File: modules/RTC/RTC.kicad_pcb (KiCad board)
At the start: 2 copper layers, 40.6 x 40.6 mm, 29 parts, among them J1 2, J10 11, J11 12, J12 13, J13 A0, J14 A1, J15 A2, J16 A3, J17 A4, J18 A5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

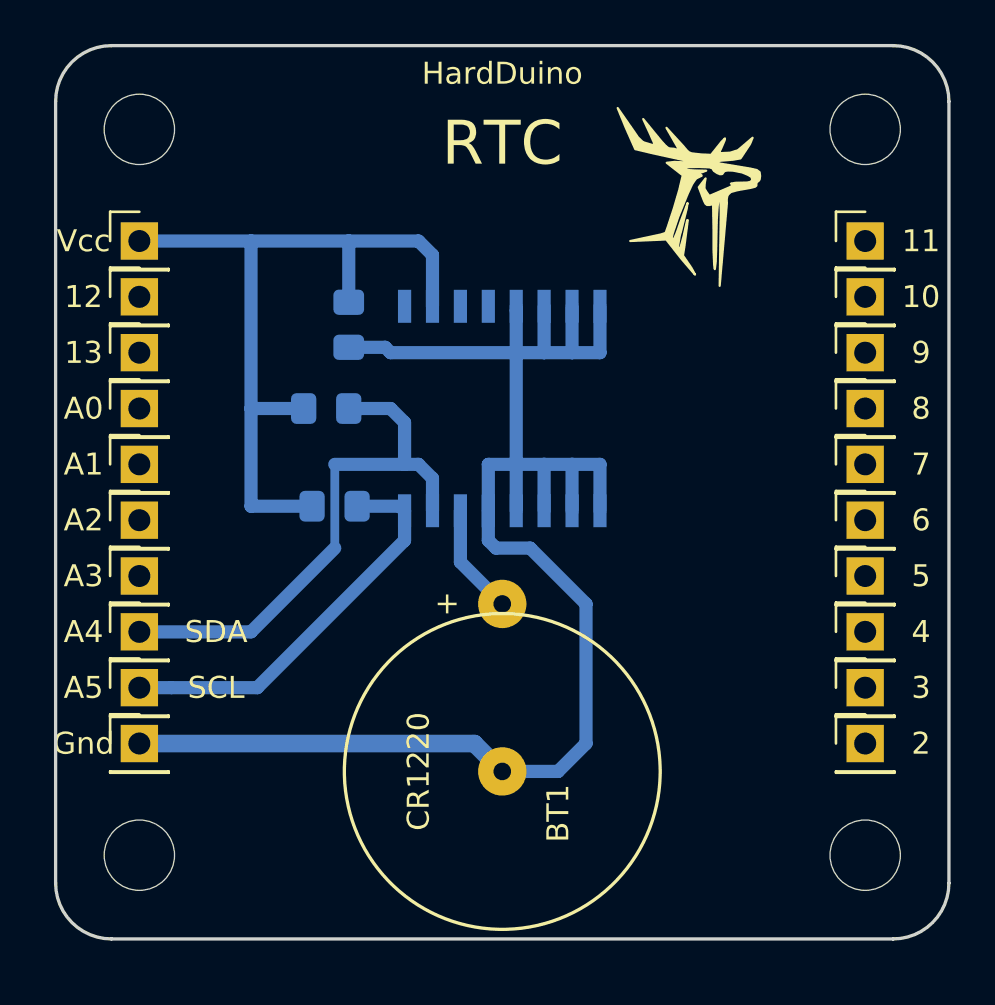
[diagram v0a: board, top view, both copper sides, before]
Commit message: 1x PCBs. Move holes to edges. Caution! This changes is uncompatible with previous versions...
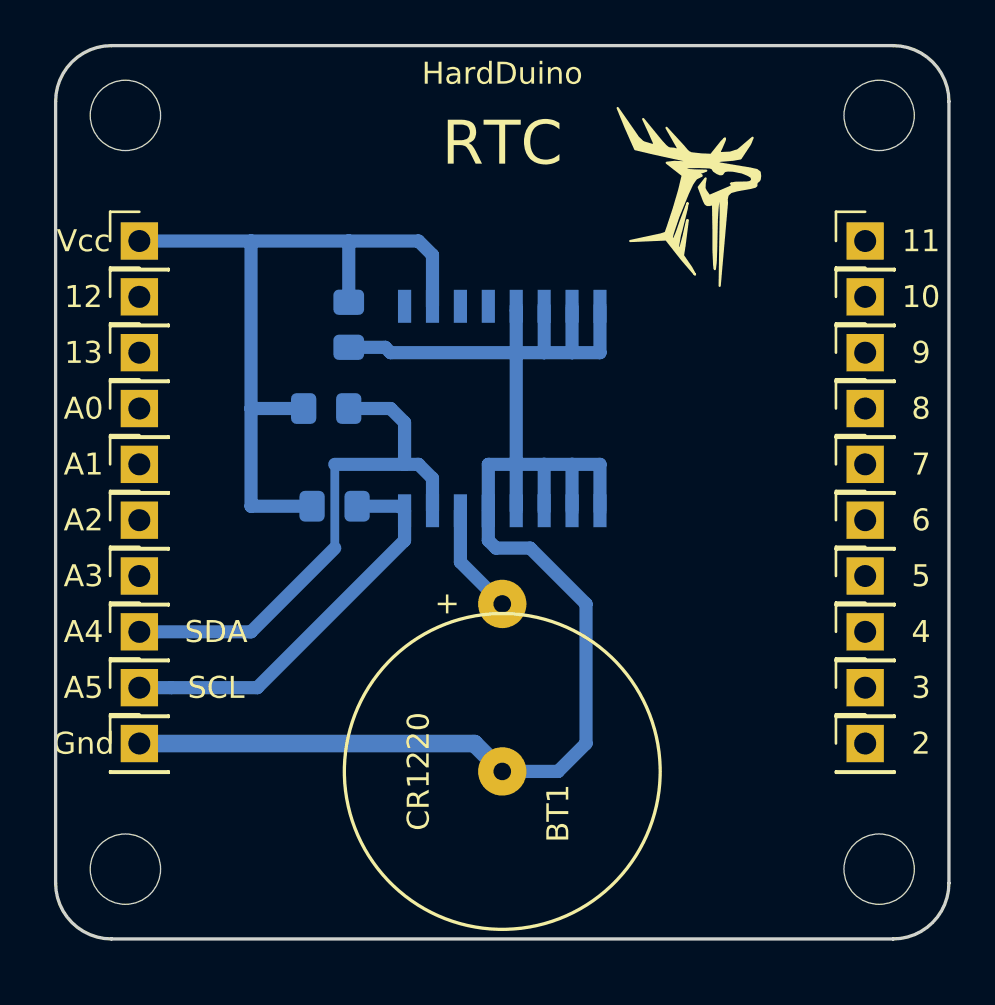
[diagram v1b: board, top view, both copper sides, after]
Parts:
- moved H2 0.90 mm to (92.1, 88.3)
- moved H4 0.90 mm to (126.4, 88.3)
- moved H1 0.90 mm to (92.1, 54.0)
- moved H3 0.90 mm to (126.4, 54.0)
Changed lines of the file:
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@@
   )
   (module MountingHole:MountingHole_3.2mm_M3 (layer F.Cu)
-    (at 92.71 54.61)
+    (at 92.0750 53.9750)
     (descr "Mounting Hole 3.2mm, no annular, M3")
     (tags "mounting hole 3.2mm no annular m3")
@@
   )
   (module MountingHole:MountingHole_3.2mm_M3 (layer F.Cu)
-    (at 92.71 87.63)
+    (at 92.0750 88.2650)
     (descr "Mounting Hole 3.2mm, no annular, M3")
     (tags "mounting hole 3.2mm no annular m3")
@@
   )
   (module MountingHole:MountingHole_3.2mm_M3 (layer F.Cu)
-    (at 125.73 54.61)
+    (at 126.3650 53.9750)
     (descr "Mounting Hole 3.2mm, no annular, M3")
     (tags "mounting hole 3.2mm no annular m3")
@@
   )
   (module MountingHole:MountingHole_3.2mm_M3 (layer F.Cu)
-    (at 125.73 87.63)
+    (at 126.3650 88.2650)
     (descr "Mounting Hole 3.2mm, no annular, M3")
     (tags "mounting hole 3.2mm no annular m3")

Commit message: Fix hash & version
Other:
- board text added: "21.02.2021"
- board text added: "b4d799"
- board text added: "v2.3"

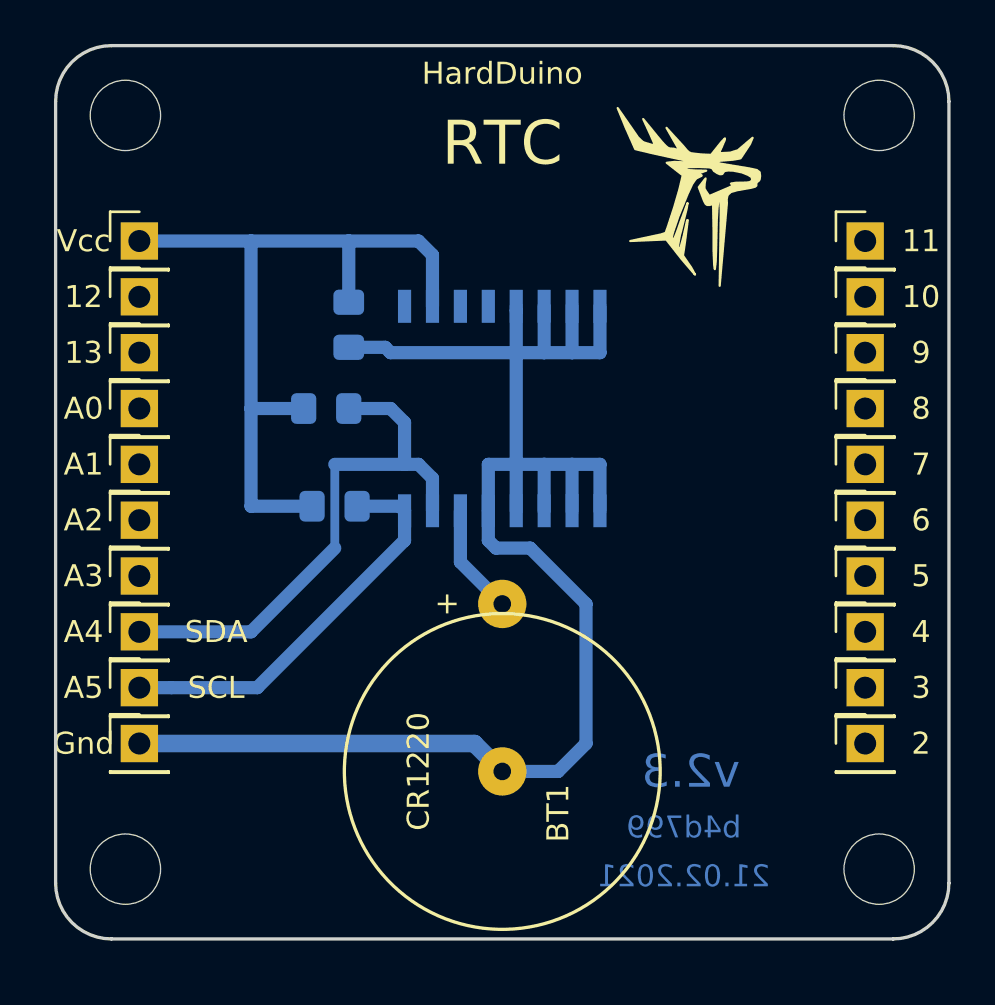
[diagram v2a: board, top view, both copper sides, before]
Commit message: All 1x shields was rotated clockwise
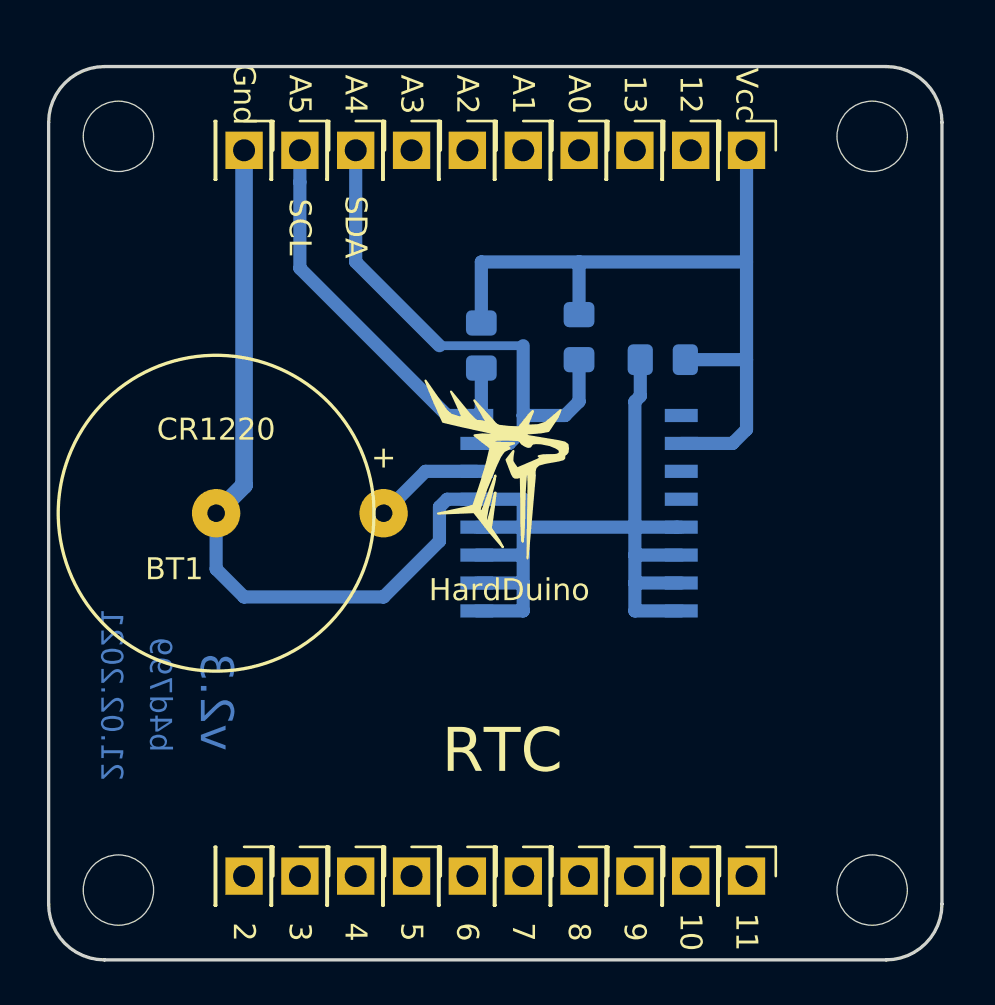
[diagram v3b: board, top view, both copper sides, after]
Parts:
- moved H3 35.2 mm to (126.0, 89.2), turned to 270 degrees
- moved H4 34.6 mm to (91.8, 89.2), turned to 270 degrees
- moved H1 34.0 mm to (126.0, 54.9), turned to 270 degrees
- moved H2 33.3 mm to (91.8, 54.9), turned to 270 degrees
- moved J10 29.4 mm to (120.3, 88.6), turned to 270 degrees
- moved J1 28.9 mm to (97.5, 88.6), turned to 270 degrees
- moved J19 27.9 mm to (120.3, 55.6), turned to 270 degrees
- moved J9 27.5 mm to (117.8, 88.6), turned to 270 degrees
- moved J20 27.4 mm to (97.5, 55.6), turned to 270 degrees
- moved J2 27.1 mm to (100.0, 88.6), turned to 270 degrees
- moved J8 26.0 mm to (115.3, 88.6), turned to 270 degrees
- moved J11 26.0 mm to (117.8, 55.6), turned to 270 degrees
- moved J3 25.7 mm to (102.6, 88.6), turned to 270 degrees
- moved J18 25.5 mm to (100.0, 55.6), turned to 270 degrees
- moved J7 24.9 mm to (112.7, 88.6), turned to 270 degrees
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
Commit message: Now all mounting holes have distance 31.92 x 31.1
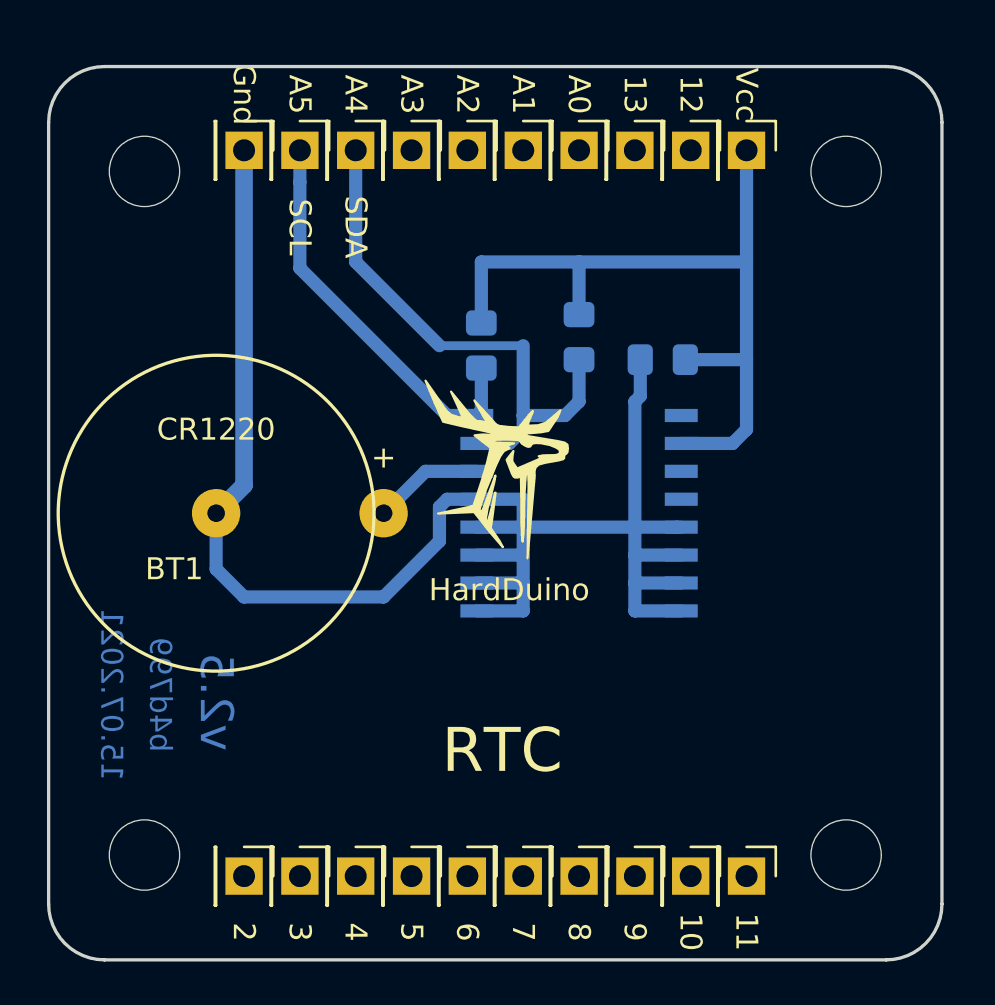
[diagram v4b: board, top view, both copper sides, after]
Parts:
- moved H1 1.99 mm to (124.9, 56.5), turned to 0 degrees
- moved H2 1.99 mm to (92.9, 56.5), turned to 0 degrees
- moved H3 1.99 mm to (124.9, 87.6), turned to 0 degrees
- moved H4 1.99 mm to (92.9, 87.6), turned to 0 degrees
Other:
- board text added: "15.07.2021"
- board text added: "v2.5"
- board text removed: "21.02.2021"
- board text removed: "v2.3"
